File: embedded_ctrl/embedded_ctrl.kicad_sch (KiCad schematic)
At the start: 19 parts, among them J1 Conn_02x13_Odd_Even, J2 DB25_Plug, J3 Conn_01x15_Socket, J4 Conn_01x15_Socket, J5 Conn_01x06, J6 Screw_Terminal_01x02, J7 USB_B, J8 Conn_01x02_Pin

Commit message: more work on embedded ctrlr
same-o
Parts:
- removed J2: DB25_Plug, Connector_Dsub:DSUB-25_Male_Horizontal_P2.77x2.54mm_EdgePinOffset9.40mm, symbol Connector:DB25_Plug
- removed J8: Conn_01x02_Pin, symbol Connector:Conn_01x02_Pin
- added C6, C7, C8: 100nF, Capacitor_SMD:C_0603_1608Metric, symbol Device:C
- added C9: 10uF, Capacitor_SMD:CP_Elec_5x5.4, symbol Device:C_Polarized
- added D1, D2, D3: D_TVS, Diode_SMD:D_0603_1608Metric, symbol Device:D_TVS
- added D4: LED, Diode_SMD:D_0603_1608Metric, symbol Device:LED
- added Q1, Q2: SS8050, Package_TO_SOT_SMD:SOT-23, symbol Transistor_BJT:SS8050
- added R10, R11, R14: 0R, Resistor_SMD:R_0603_1608Metric, symbol Device:R
- added R12, R13, R5: 10k, Resistor_SMD:R_0603_1608Metric, symbol Device:R
- added R15, R8: 2k (5%), Resistor_SMD:R_0603_1608Metric, symbol Device:R
- added R6: 22.1k (1%), Resistor_SMD:R_0603_1608Metric, symbol Device:R
- added R7: 47.5k (1%), Resistor_SMD:R_0603_1608Metric, symbol Device:R
- added R9: DNP, Resistor_SMD:R_0603_1608Metric, symbol Device:R
- added TP1: VBUS, symbol Connector:TestPoint
- added U1: ESP32-WROOM-32, RF_Module:ESP32-WROOM-32, symbol RF_Module:ESP32-WROOM-32
- added U2: CP2102N-A02-GQFN28, Package_DFN_QFN:QFN-28-1EP_5x5mm_P0.5mm_EP3.35x3.35mm, symbol Interface_USB:CP2102N-Axx-xQFN28
- added U3: R-78E3.3-1.0, Converter_DCDC:Converter_DCDC_RECOM_R-78E-0.5_THT, symbol Regulator_Switching:R-78E3.3-1.0
- C1, C2, C3, C4: JLCPCB Part # (none) -> C14663
- C5: footprint Capacitor_SMD:CP_Elec_5x5.8 -> Capacitor_SMD:CP_Elec_5x5.4; JLCPCB Part # (none) -> C72487
- J1: JLCPCB Part # (none) -> C2894993
- J3, J4: footprint Connector_PinSocket_2.54mm:PinSocket_1x15_P2.54mm_Vertical -> (none); now not fitted
- J6: JLCPCB Part # (none) -> C8465
- J7: footprint (none) -> Connector_USB:USB_B_OST_USB-B1HSxx_Horizontal; JLCPCB Part # (none) -> C720549
- R1, R2, R3, R4: JLCPCB Part # (none) -> C25804
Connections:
- net 3V3: now also C7.1, C8.1, R5.1, R8.1, U1.2 (VDD), U2.6 (VDD), U2.7 (VREGIN), U3.3 (OUT)
- net 5V: now also C9.1, R15.1, U3.1 (IN); no longer J4.1 (Pin_1)
- net D12: now also U1.14 (IO12)
- net D14: now also U1.13 (IO14)
- net D15: now also U1.23 (IO15)
- net D18: now also U1.30 (IO18)
- net D19: now also U1.31 (IO19)
- net D22: now also U1.36 (IO22)
- net D23: now also U1.37 (IO23)
- net D25: now also U1.10 (IO25)
- net D26: now also U1.11 (IO26)
- net D27: now also U1.12 (IO27)
- net D32: now also U1.8 (IO32)
- net D33: now also U1.9 (IO33)
- net D34: now also U1.6 (IO34)
- net D35: now also U1.7 (IO35)
- net D5: now also U1.29 (IO5)
- net EN: now also C6.1, Q1.3 (C), R5.2, U1.3 (EN)
- net GND: now also C6.2, C7.2, C8.2, C9.2, D1.1 (A1), D2.1 (A1), D3.1 (A1), D4.1 (K), R7.1, R9.2, U1.1 (GND), U1.15 (GND), U1.38 (GND), U1.39 (GND), U2.29 (GND), U2.3 (GND), U3.2 (GND)
- net D-: now reaches J7.2 (D-)
- net D-: now also D1.2 (A2), U2.5 (D-)
- net D+: now reaches J7.3 (D+)
- net D+: now also D2.2 (A2), U2.4 (D+)
- net VBUS: now reaches J7.1 (VBUS)
- net VBUS: now also D3.2 (A2), R6.1, TP1.1
- new net: R6.2, R7.2, U2.8 (VBUS)
- new net: Q1.1 (B), R12.2
- new net: D4.2 (A), R15.2
- new net: R9.1, U2.11 (~{SUSPEND})
- new net: R8.2, U2.9 (~{RST})
- new net: Q2.2 (E), R14.1
- new net: Q2.1 (B), R13.2
- new net IO0: Q2.3 (C), U1.25 (IO0)
- new net RXD0_ESP: R11.1, U1.34 (RXD0/IO3)
- new net RXD_BRIDGE: R10.2, U2.25 (RXD)
- new net TXD0_ESP: R10.1, U1.35 (TXD0/IO1)
- new net TXD_BRIDGE: R11.2, U2.26 (TXD)
- new net U1RXD: U1.17 (SHD/SD2)
- new net U1TXD: U1.18 (SWP/SD3)
- new net U2RXD: U1.27 (IO16)
- new net U2TXD: U1.28 (IO17)
- new net VIN: J4.1 (Pin_1)
- new net ~{DTR}: R12.1, R14.2, U2.28 (~{DTR})
- new net ~{RTS}: Q1.2 (E), R13.1, U2.24 (~{RTS})
- no-connect marks 5 -> 28
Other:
- note added: "Connector to Motherboard"
- note added: "Inputs"
- note added: "MCU"
- note added: "Mechanical"
- note added: "Outputs"
- note added: "Pendant connector"
- note added: "Pin assignment"
- note added: "Power Input"
- note added: "RJ11 conn: C189737"
- note added: "USB port & USB-to-UART"
- note added: "simplifies the layout"
- moved on the sheet: C1, C2, C3, C4, C5, H1, H2, J1, J5, J6, J7, R1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

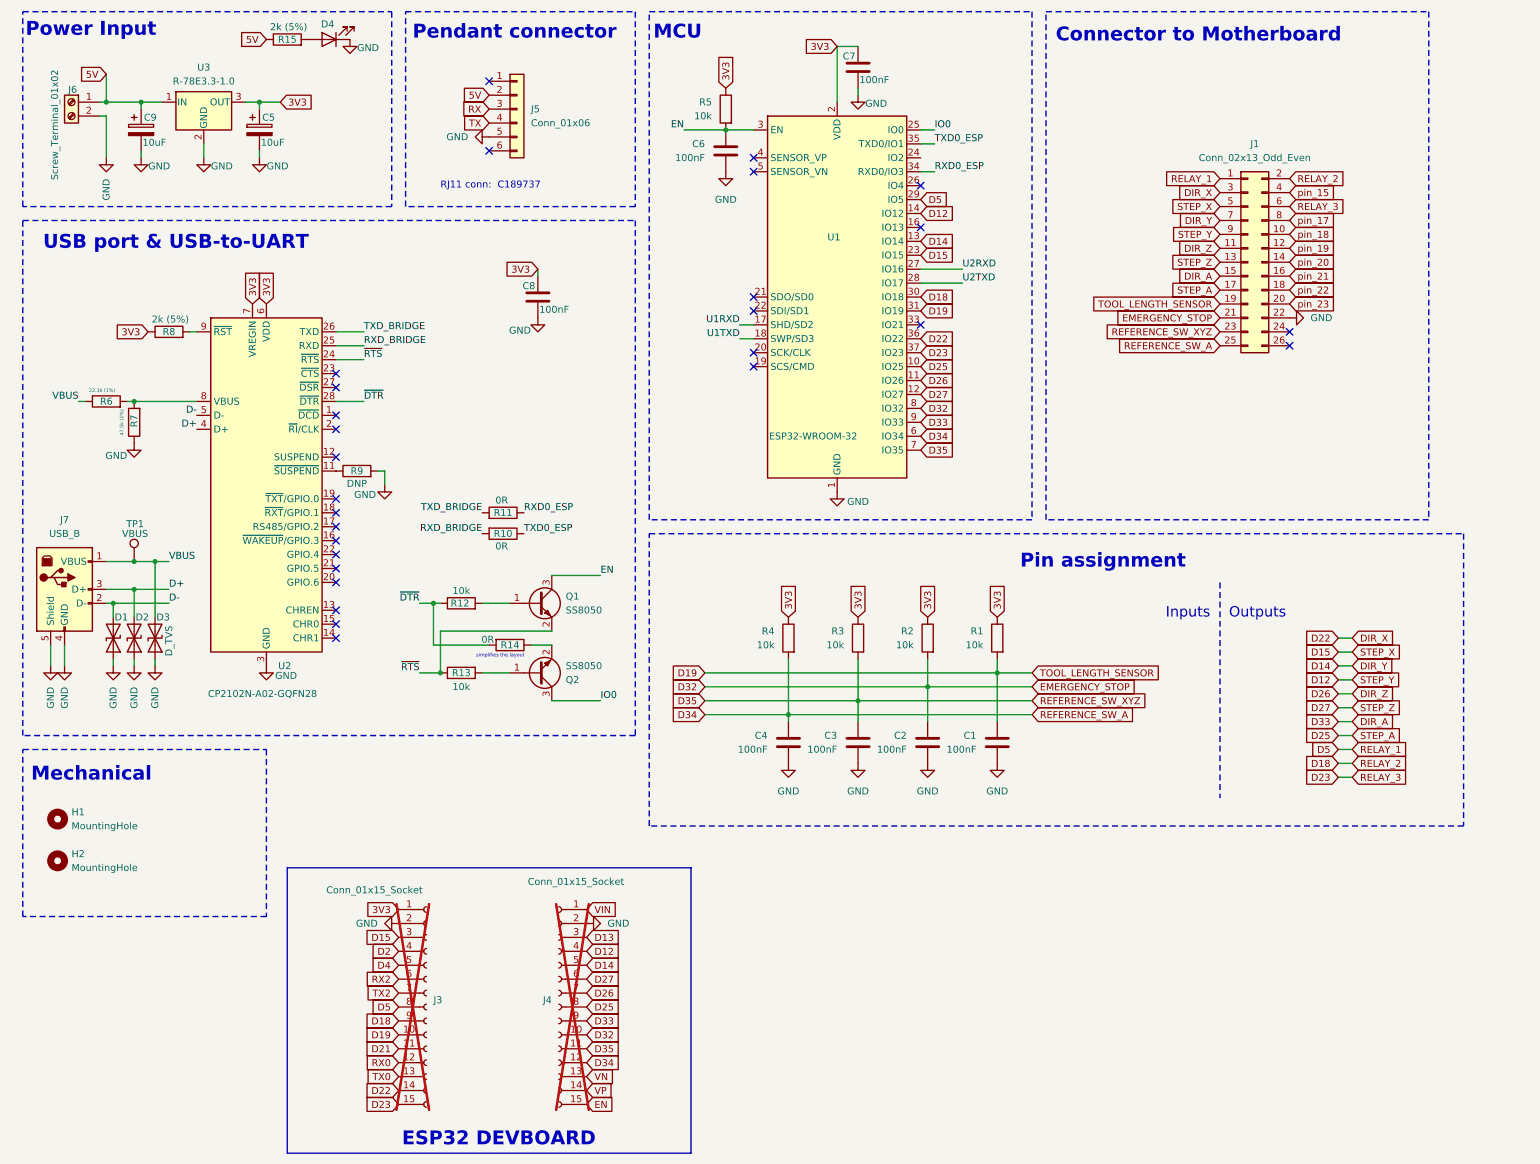
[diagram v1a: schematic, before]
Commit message: add rj11 connectors for pendants
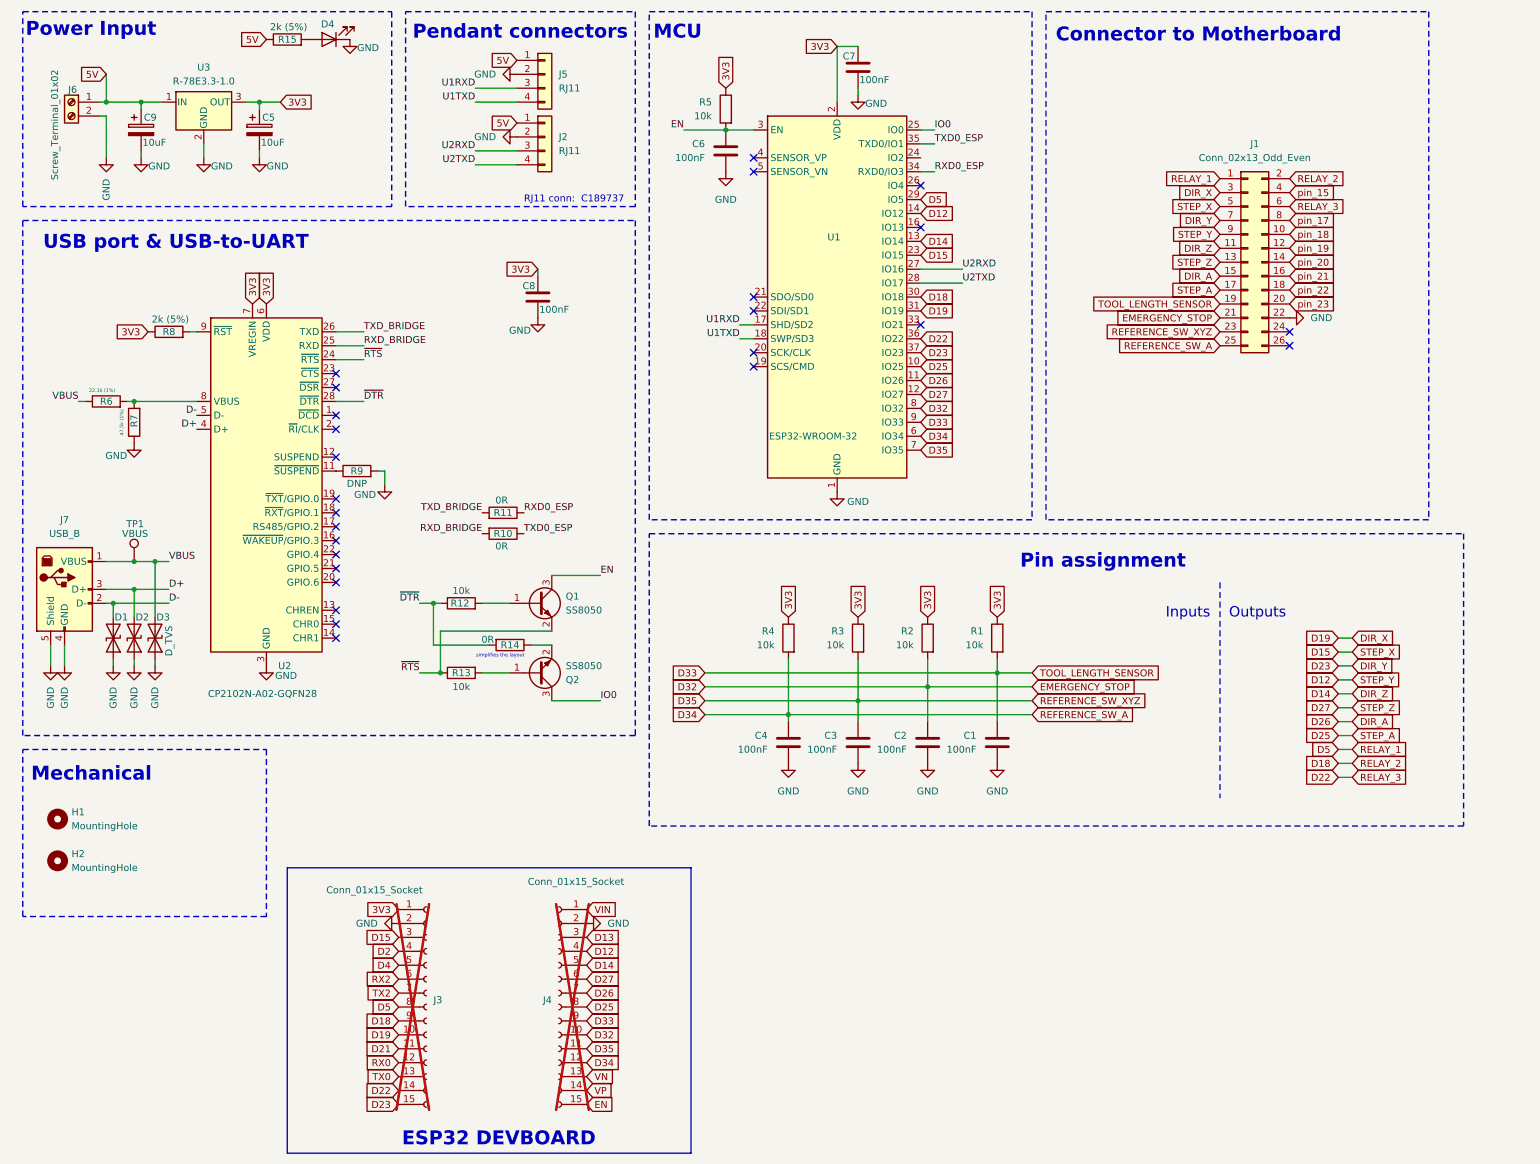
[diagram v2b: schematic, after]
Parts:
- added J2: RJ11, Library:RJ11_C189737, symbol Connector_Generic:Conn_01x04
- J5: value Conn_01x06 -> RJ11; footprint (none) -> Library:RJ11_C189737; symbol Connector_Generic:Conn_01x06 -> Connector_Generic:Conn_01x04
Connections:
- net RX is gone; now on net U1RXD: J5.3 (Pin_3)
- net TX is gone; now on net U1TXD: J5.4 (Pin_4)
- net 5V: now also J5.1 (Pin_1), J2.1 (Pin_1); no longer J5.2 (Pin_2)
- net D14: now also J1.11 (Pin_11); no longer J1.7 (Pin_7)
- net D19: now also J1.3 (Pin_3); no longer C1.1, J1.19 (Pin_19), R1.2
- net D22: now also J1.6 (Pin_6); no longer J1.3 (Pin_3)
- net D23: now also J1.7 (Pin_7); no longer J1.6 (Pin_6)
- net D26: now also J1.15 (Pin_15); no longer J1.11 (Pin_11)
- net D33: now also C1.1, J1.19 (Pin_19), R1.2; no longer J1.15 (Pin_15)
- net GND: now also J5.2 (Pin_2), J2.2 (Pin_2); no longer J5.5 (Pin_5)
- net U2RXD: now also J2.3 (Pin_3)
- net U2TXD: now also J2.4 (Pin_4)
- no-connect marks 28 -> 26
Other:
- note added: "Pendant connectors"
- note removed: "Pendant connector"

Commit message: same
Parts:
- added TP2: 3V3, TestPoint:TestPoint_THTPad_D1.0mm_Drill0.5mm, symbol Connector:TestPoint
- added TP3: 5V, TestPoint:TestPoint_THTPad_D1.0mm_Drill0.5mm, symbol Connector:TestPoint
- added TP4: GND, TestPoint:TestPoint_THTPad_D1.0mm_Drill0.5mm, symbol Connector:TestPoint
- TP1: footprint (none) -> TestPoint:TestPoint_THTPad_D1.0mm_Drill0.5mm
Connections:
- net 3V3: now also TP2.1
- net 5V: now also TP3.1
- net GND: now also TP4.1

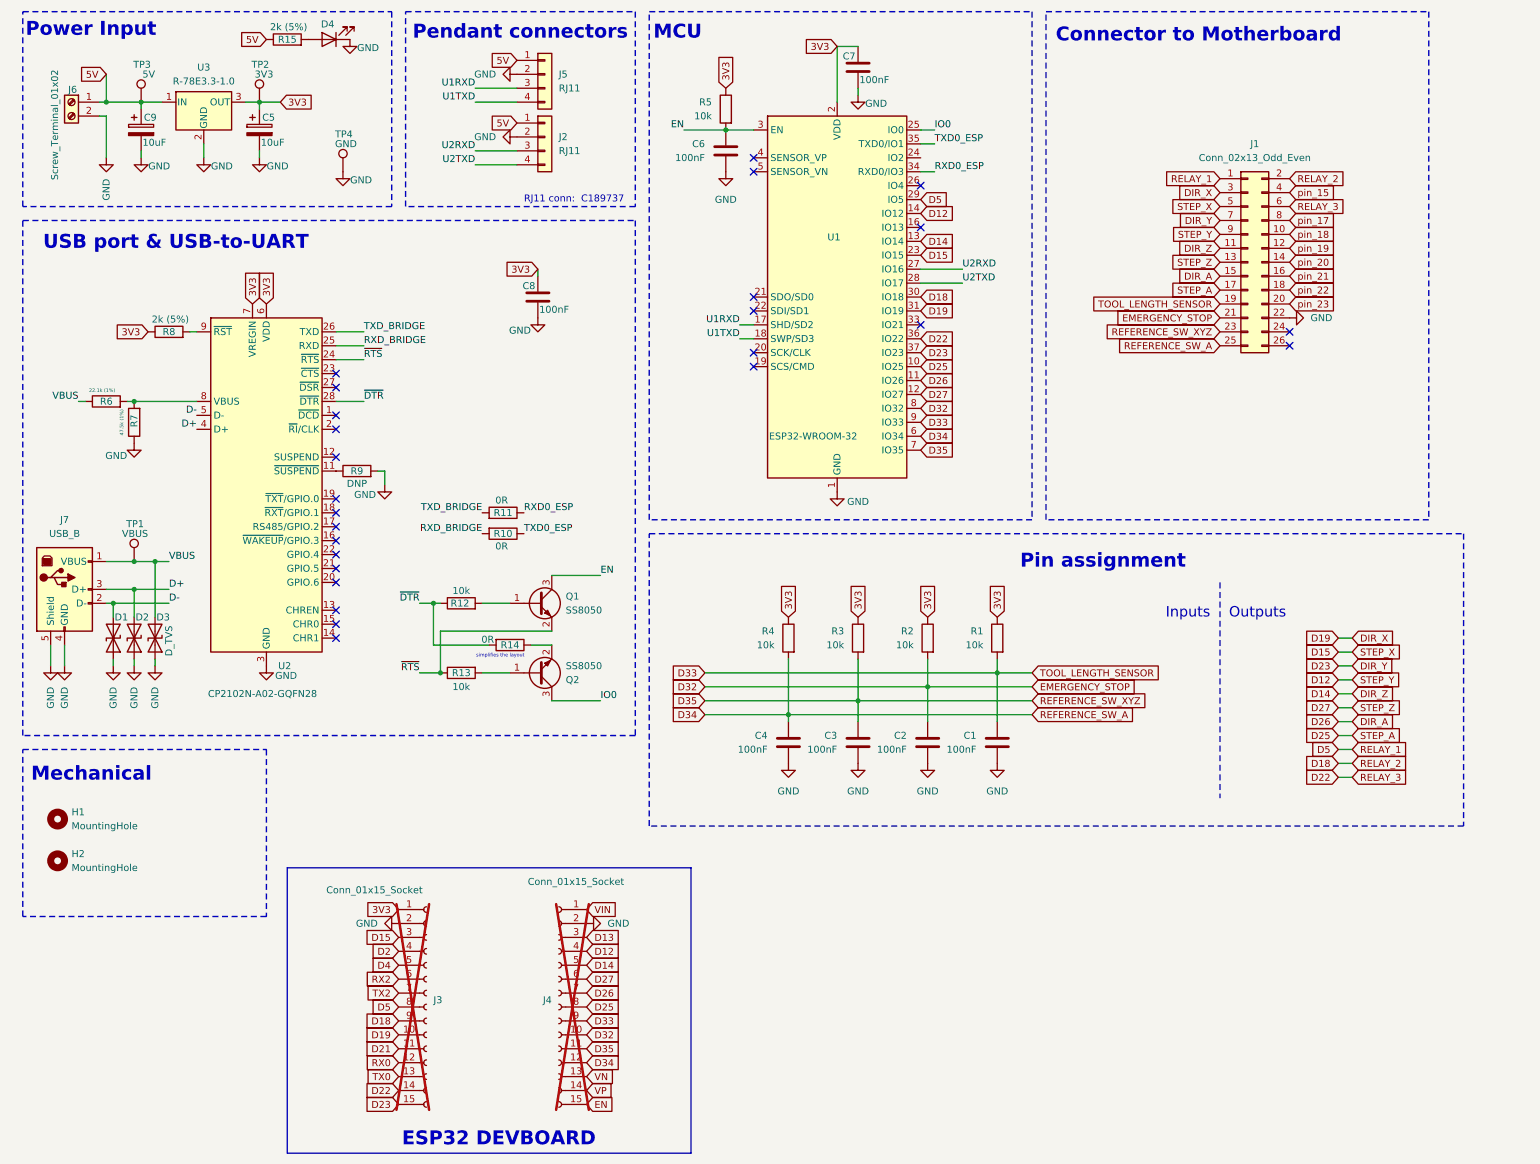
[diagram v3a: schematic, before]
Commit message: Reassign pins to free up JTAG pins, just in case
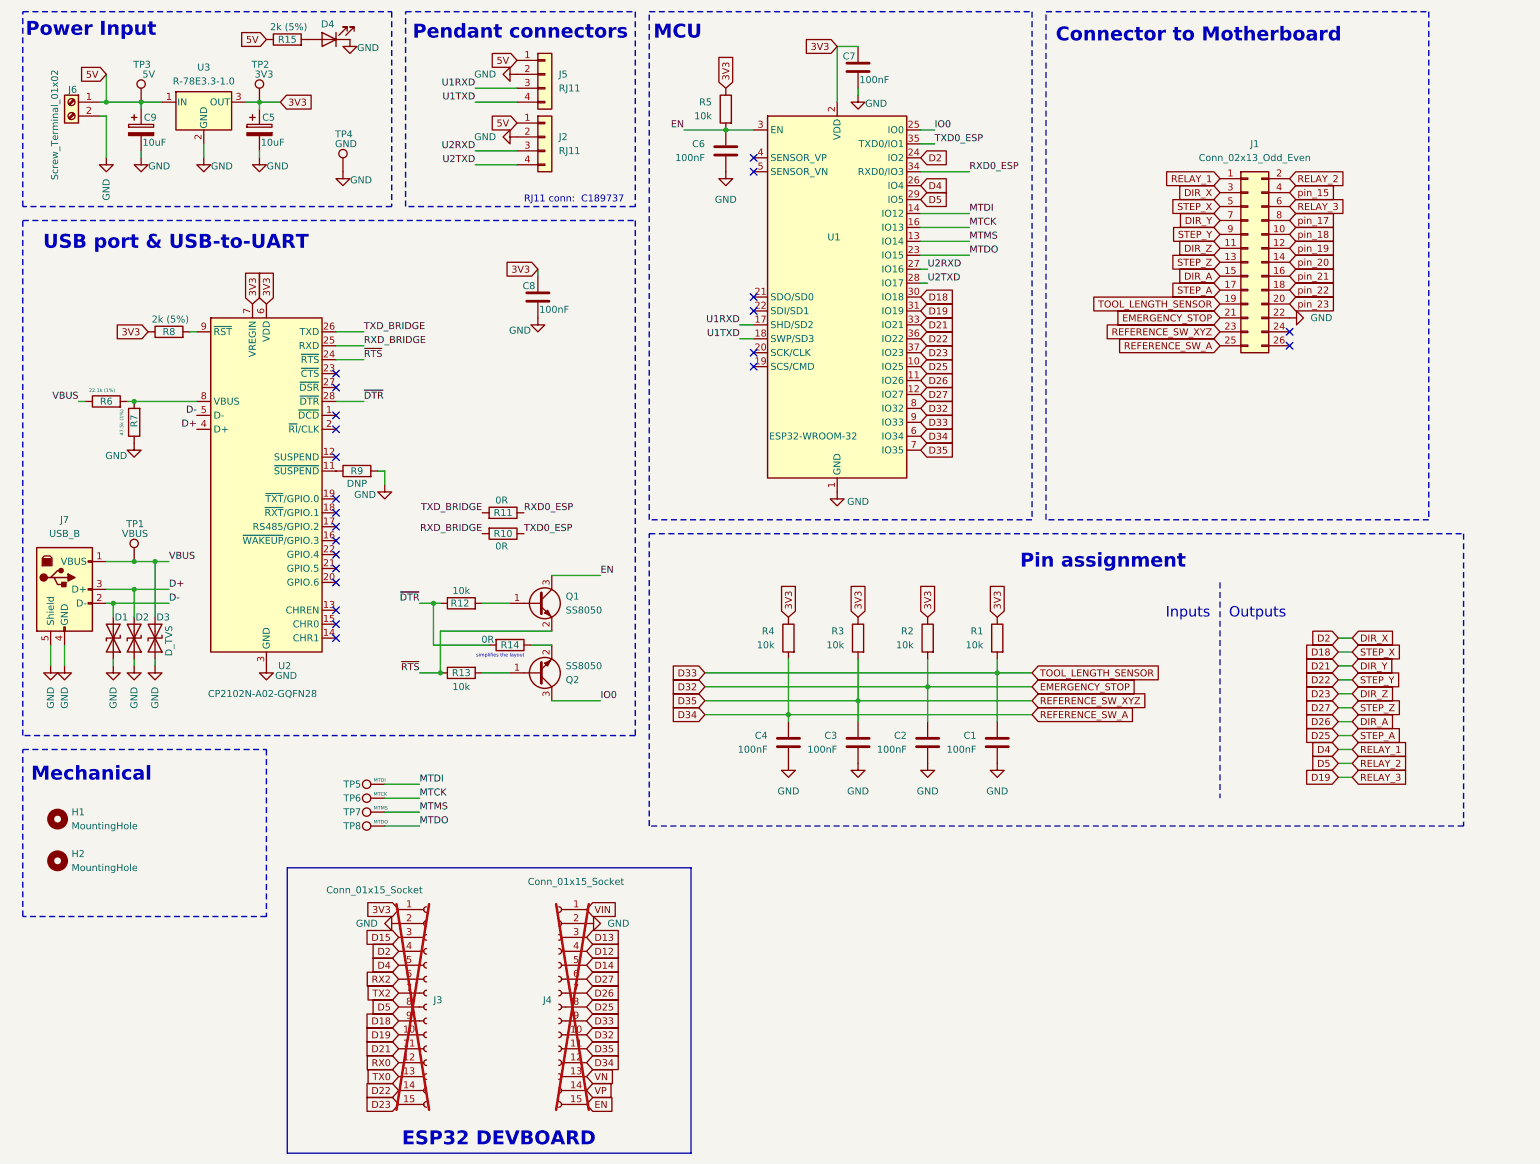
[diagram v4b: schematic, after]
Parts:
- added TP5: MTDI, TestPoint:TestPoint_Pad_D1.0mm, symbol Connector:TestPoint
- added TP6: MTCK, TestPoint:TestPoint_Pad_D1.0mm, symbol Connector:TestPoint
- added TP7: MTMS, TestPoint:TestPoint_Pad_D1.0mm, symbol Connector:TestPoint
- added TP8: MTDO, TestPoint:TestPoint_Pad_D1.0mm, symbol Connector:TestPoint
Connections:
- net D12: no longer J1.9 (Pin_9), U1.14 (IO12)
- net D14: no longer J1.11 (Pin_11), U1.13 (IO14)
- net D15: no longer J1.5 (Pin_5), U1.23 (IO15)
- net D18: now also J1.5 (Pin_5); no longer J1.2 (Pin_2)
- net D19: now also J1.6 (Pin_6); no longer J1.3 (Pin_3)
- net D2: now also J1.3 (Pin_3), U1.24 (IO2)
- net D21: now also J1.7 (Pin_7), U1.33 (IO21)
- net D22: now also J1.9 (Pin_9); no longer J1.6 (Pin_6)
- net D23: now also J1.11 (Pin_11); no longer J1.7 (Pin_7)
- net D4: now also J1.1 (Pin_1), U1.26 (IO4)
- net D5: now also J1.2 (Pin_2); no longer J1.1 (Pin_1)
- net MTCK: now reaches U1.16 (IO13)
- net MTCK: now also TP6.1
- new net MTDI: TP5.1, U1.14 (IO12)
- new net MTDO: TP8.1, U1.23 (IO15)
- new net MTMS: TP7.1, U1.13 (IO14)
- no-connect marks 26 -> 23
